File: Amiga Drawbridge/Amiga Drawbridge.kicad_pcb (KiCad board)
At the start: 2 copper layers, 90 x 94 mm, 0 parts

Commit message: Added metal details
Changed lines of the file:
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@@
   (general
     (thickness 1.6)
-    (drawings 154)
+    (drawings 167)
     (tracks 0)
     (zones 0)
@@
       (padsonsilk false)
       (subtractmaskfromsilk false)
-      (outputformat 1)
+      (outputformat 4)
       (mirror false)
-      (drillshape 1)
+      (drillshape 0)
       (scaleselection 1)
-      (outputdirectory ""))
+      (outputdirectory "export/"))
   )
   (net 0 "")
@@
     (uvia_drill 0.1)
   )
+  (gr_poly (pts (xy 155.7 87.3) (xy 157.8 87.9) (xy 159.5 88.8) (xy 161.3 90.1) (xy 162.4 91.3) (xy 163.1 92.1) (xy 163.8 93.2) (xy 164.2 94) (xy 147.1 88.5) (xy 148.4 87.9) (xy 150.3 87.3) (xy 152 87) (xy 153.6 87)) (layer B.SilkS) (width 0.1))
+  (gr_poly (pts (xy 150.5 98.7) (xy 150.4 99.1) (xy 150.5 99.4) (xy 150.615185 99.711237) (xy 150.8 100) (xy 147.6 100) (xy 147.953637 98.530233) (xy 148 98.2) (xy 150.8 98.2)) (layer B.SilkS) (width 0.1))
+  (gr_poly (pts (xy 164.2 94) (xy 165.1 96.3) (xy 165.5 98.9) (xy 165.3 101.7) (xy 164.8 103.7) (xy 146.530132 103.842824) (xy 146.7 103.2) (xy 147.2 101.4) (xy 147.6 100) (xy 150.8 100) (xy 151.615185 101.443288) (xy 151.9 101.8) (xy 152.3 102) (xy 152.8 102.1) (xy 153.1 102) (xy 153.5 101.8) (xy 155.2 100.8) (xy 155.4 100.6) (xy 155.6 100.3) (xy 155.7 99.8) (xy 155.6 99.4) (xy 155.3 98.8) (xy 154.4 97.3) (xy 154.1 97) (xy 153.5 96.8) (xy 153 96.9) (xy 150.8 98.2) (xy 148 98.2) (xy 147.9 97.7) (xy 147.8 97.5) (xy 147.5 97.2) (xy 147.069753 96.999301) (xy 147.1 88.5)) (layer B.SilkS) (width 0.1))
+  (gr_poly (pts (xy 143.2 98.9) (xy 142.312875 102.195177) (xy 142.2 102.7) (xy 142.5 103.6) (xy 142.8 103.9) (xy 143.2 104.2) (xy 143.8 104.4) (xy 144.9 104.7) (xy 145.3 104.8) (xy 145.8 104.7) (xy 146.1 104.5) (xy 146.4 104.2) (xy 146.530132 103.842824) (xy 164.8 103.7) (xy 163.8 105.7) (xy 162.6 107.5) (xy 161.4 108.7) (xy 160 109.9) (xy 158.5 110.7) (xy 157.4 111.2) (xy 155.7 111.7) (xy 154.4 111.9) (xy 152.8 112) (xy 151.2 111.9) (xy 149.7 111.6) (xy 148.1 111) (xy 146.7 110.3) (xy 145.1 109.2) (xy 143.7 107.9) (xy 142.7 106.6) (xy 141.8 105.1) (xy 141.2 103.6) (xy 140.7 102) (xy 140.5 100.6) (xy 140.5 98.9) (xy 140.7 97.4) (xy 143.6 97.4)) (layer B.SilkS) (width 0.1))
+  (gr_poly (pts (xy 147.069753 96.999301) (xy 145.3 96.5) (xy 144.8 96.4) (xy 144.2 96.6) (xy 143.8 96.9) (xy 143.60697 97.365549) (xy 143.6 97.4) (xy 140.7 97.4) (xy 141.2 95.4) (xy 141.9 93.8) (xy 142.9 92.2) (xy 143.6 91.3) (xy 145.8 89.3) (xy 147.1 88.5)) (layer B.SilkS) (width 0.1))
+  (gr_poly (pts (xy 176 117.6) (xy 176.4 118) (xy 176.5 118.5) (xy 176.5 144.5) (xy 171.5 144.5) (xy 171.5 146) (xy 148.5 146) (xy 148.5 120) (xy 148.7 117.5) (xy 175.5 117.5)) (layer B.SilkS) (width 0.1))
+  (gr_poly (pts (xy 148.7 120) (xy 148.5 120) (xy 148.5 119.8) (xy 148.3 119.6) (xy 148 119.5) (xy 136.8 119.5) (xy 136.6 119.7) (xy 136.5 120) (xy 136.5 144.1) (xy 136.7 144.4) (xy 137 144.5) (xy 140.5 144.5) (xy 140.5 146) (xy 144.5 146) (xy 144.5 144.5) (xy 148.2 144.5) (xy 148.4 144.3) (xy 148.5 144) (xy 148.5 146) (xy 175 146) (xy 175 144.5) (xy 176.5 144.5) (xy 176.5 149) (xy 129.5 149) (xy 129.5 118.3) (xy 129.6 118.1) (xy 129.8 117.8) (xy 130.1 117.6) (xy 130.5 117.5) (xy 148.7 117.5)) (layer B.SilkS) (width 0.1))
+  (gr_poly (pts (xy 194.5 137.5) (xy 196 137.5) (xy 193.5 143) (xy 191 137.5) (xy 192.5 137.5) (xy 192.5 135) (xy 194.5 135)) (layer F.SilkS) (width 0.1))
+  (gr_poly (pts (xy 175.9 117.6) (xy 176.2 117.8) (xy 176.4 118.1) (xy 176.5 118.5) (xy 176.5 149) (xy 171.5 149) (xy 171.5 148.5) (xy 168.5 148.5) (xy 168.5 149) (xy 149.5 149) (xy 149.5 117.5) (xy 175.5 117.5)) (layer F.SilkS) (width 0.1))
+  (gr_poly (pts (xy 149.5 149) (xy 137 149) (xy 137 144.5) (xy 148 144.5) (xy 148.3 144.4) (xy 148.5 144.2) (xy 148.5 120) (xy 148.4 119.7) (xy 148.2 119.5) (xy 137 119.5) (xy 137 117.5) (xy 149.5 117.5)) (layer F.SilkS) (width 0.1))
+  (gr_poly (pts (xy 136.6 144.3) (xy 136.8 144.5) (xy 137 144.5) (xy 137 149) (xy 136.5 149) (xy 136.5 144)) (layer F.SilkS) (width 0.1))
+  (gr_poly (pts (xy 137 119.5) (xy 136.8 119.5) (xy 136.6 119.7) (xy 136.5 120) (xy 136.5 117.5) (xy 137 117.5)) (layer F.SilkS) (width 0.1))
+  (gr_poly (pts (xy 136.5 119.4) (xy 136.5 120) (xy 136.5 149) (xy 129.5 149) (xy 129.5 118.5) (xy 129.6 118) (xy 130 117.6) (xy 130.5 117.5) (xy 136.5 117.5)) (layer F.SilkS) (width 0.1))
   (gr_line (start 194.5 135) (end 194.5 137.5) (layer F.SilkS) (width 0.12))
   (gr_line (start 192.5 135) (end 194.5 135) (layer F.SilkS) (width 0.12))
@@
   (gr_line (start 153.322716 101.90082) (end 155.054767 100.90082) (layer B.SilkS) (width 0.12))
   (gr_line (start 150.615185 99.711237) (end 151.615185 101.443288) (layer B.SilkS) (width 0.12))
-  (gr_circle (center 153 99.5) (end 140.5 99.5) (layer B.SilkS) (width 0.12))
+  (gr_circle (center 153 99.5) (end 165.5 99.5) (layer B.SilkS) (width 0.3))
   (gr_circle (center 153 100) (end 166.5 100) (layer B.SilkS) (width 0.3))
   (gr_line (start 194 55.5) (end 192.5 55.5) (layer B.SilkS) (width 0.12))

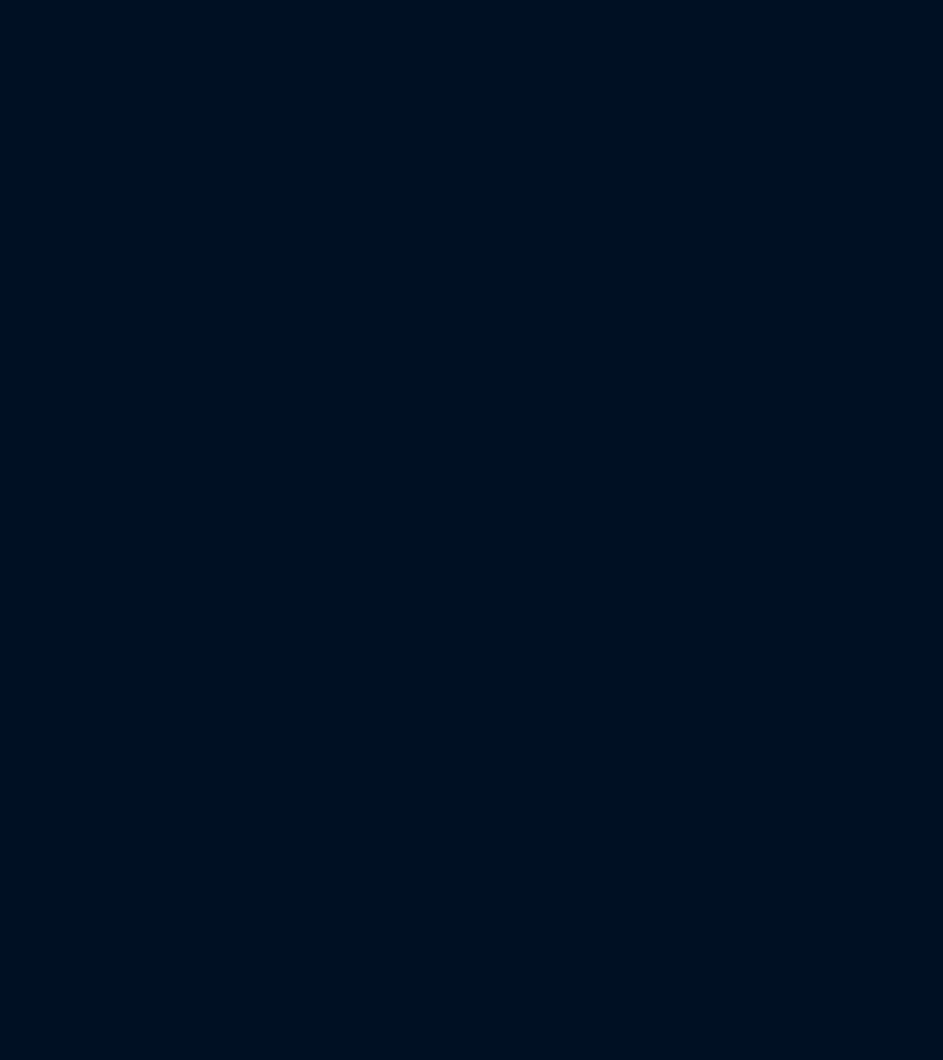
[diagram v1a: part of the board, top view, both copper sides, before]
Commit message: Arduino Pro Mini footprint
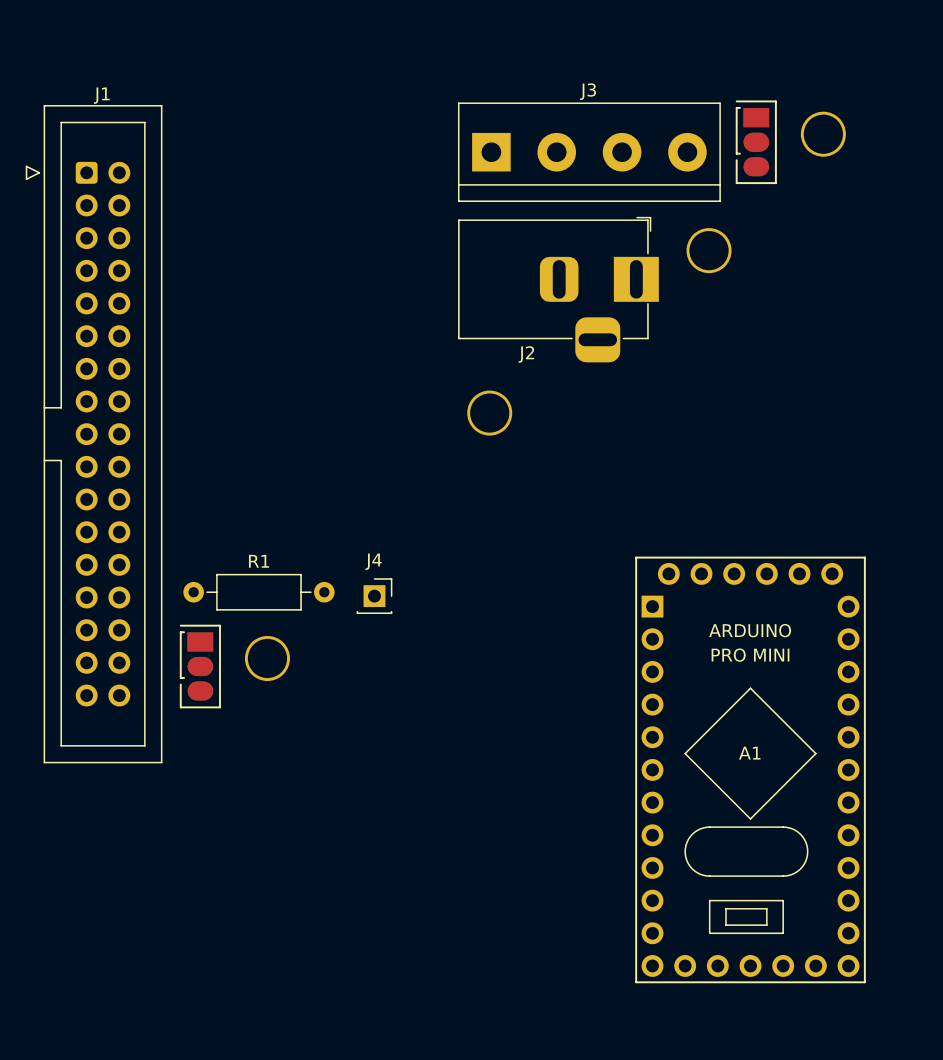
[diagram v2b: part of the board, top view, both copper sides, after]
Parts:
- added A1: ARDUINO, arduino:Arduino_Pro_Mini, F.Cu at (82.5, 121.9)
- added J1: FDC, Connector_IDC:IDC-Header_2x17_P2.54mm_Vertical, F.Cu at (30.9, 74.2)
- added J2: PWR_EXT, Connector_BarrelJack:BarrelJack_Horizontal, F.Cu at (73.7, 82.5)
- added J3: PWR_DRV, TerminalBlock:TerminalBlock_bornier-4_P5.08mm, F.Cu at (62.4, 72.6)
- added J4: 12v, Connector_PinSocket_2.54mm:PinSocket_1x01_P2.54mm_Vertical, F.Cu at (53.3, 107.1)
- added JP1: ARD_TYPE, solder_bridge:select, F.Cu at (39.8, 110.7)
- added JP2: PWR_SEL, solder_bridge:select, F.Cu at (83.0, 69.9)
- added M1: Mounting, mounting:M3, F.Cu at (62.3, 92.9)
- added M2: Mounting, mounting:M3, F.Cu at (79.3, 80.3)
- added M3: Mounting, mounting:M3, F.Cu at (88.2, 71.2)
- added M4: Mounting, mounting:M3, F.Cu at (45.0, 112.0)
- added R1: 1k, Resistor_THT:R_Axial_DIN0207_L6.3mm_D2.5mm_P10.16mm_Horizontal, F.Cu at (39.3, 106.8)

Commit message: Routed tracks
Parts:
- added A2: FT232RL, ft232rl:FT232RL, F.Cu at (130.5, 92.1)
- A1: value ARDUINO -> Arduino_Pro_Mini
- J3: footprint TerminalBlock:TerminalBlock_bornier-4_P5.08mm -> pwr_drv:PWR_DRV
- J4: footprint Connector_PinSocket_2.54mm:PinSocket_1x01_P2.54mm_Vertical -> Connector_PinHeader_2.54mm:PinHeader_1x01_P2.54mm_Vertical
- M1, M2, M3, M4: footprint mounting:M3 -> mounting:M3_pin
- moved JP1 154.6 mm to (193.0, 90.2)
- moved J4 144.8 mm to (193.5, 71.0)
- moved J1 143.1 mm to (173.3, 59.7), turned to 270 degrees
- moved M2 125.3 mm to (193.5, 132.0)
- moved J3 120.1 mm to (182.0, 62.0)
- moved M3 105.6 mm to (193.5, 62.5)
- moved R1 93.9 mm to (128.3, 76.8)
- moved A1 93.2 mm to (170.8, 92.1), turned to 270 degrees
- moved M4 83.7 mm to (112.5, 62.5)
- moved M1 63.6 mm to (112.5, 132.0)
- moved J2 50.0 mm to (121.9, 69.2), turned to 270 degrees
- moved JP2 41.4 mm to (123.8, 76.8), turned to 270 degrees
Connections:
- A1 pad 24: (no net) -> /CTS
- A1 pad 25: (no net) -> /~REDWC
- A1 pad 26: (no net) -> VCC
- A1 pad 28: (no net) -> GND
- A1 pad 3: Net-(A1-Pad3) -> (no net)
- A1 pad 30: (no net) -> Net-(A1-Pad30)
- A1 pad 35: (no net) -> Net-(A1-Pad35)
- J1 pad 2: (no net) -> /~REDWC
- JP1 pad 1: (no net) -> Net-(A1-Pad35)
- JP1 pad 2: (no net) -> /DTR
- JP1 pad 3: (no net) -> Net-(A1-Pad30)
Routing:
- net VCC: track 0.00 -> 84.8 mm, vias 0 -> 2
- net /TXO: track 0.00 -> 81.3 mm
- net Net-(J3-Pad1): track 0.00 -> 78.1 mm
- net /DTR: track 0.00 -> 76.9 mm, vias 0 -> 1
- net /CTS: track 0.00 -> 67.9 mm, vias 0 -> 3
- net /RXI: track 0.00 -> 67.9 mm
- net /~DRVSB: track 0.00 -> 59.7 mm
- net /~WPT: track 0.00 -> 58.1 mm, vias 0 -> 3
- net /~RDATA: track 0.00 -> 57.1 mm
- net /~WGATE: track 0.00 -> 53.9 mm, vias 0 -> 3
- net /~DSKCHG: track 0.00 -> 52.7 mm
- net /~WDATA: track 0.00 -> 46.7 mm
- net /~TRK00: track 0.00 -> 39.5 mm
- net /~REDWC: track 0.00 -> 39.1 mm, vias 0 -> 1
- net /~SIDE1: track 0.00 -> 34.9 mm
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- added copper zone on B.Cu, net GND
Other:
- net class Power added: clearance 0.2, trace_width 0.381, via_dia 1, via_drill 0.4
- rule trace_min: 0.2 -> 0
- board text added: "12V"
- board text added: "5V"
- board text added: "ARD_TYPE: 1-2 DTR TXO RXI VCC GND GND (A) 2-3 GND GND VCC RXI TXO DTR (B)"
- board text added: "GND"
- board text added: "PWR_SEL: 1-2 USB 2-3 5v barrel jack"

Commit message: Exported files
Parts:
- added REF**: OSHW-Logo_7.5x8mm_SilkScreen, Symbol:OSHW-Logo_7.5x8mm_SilkScreen, F.Cu at (153.0, 76.0)
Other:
- board text added: "Amiga DrawBridge github.com/tebl"
